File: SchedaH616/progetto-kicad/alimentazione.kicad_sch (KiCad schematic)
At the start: 53 parts, among them J103 DC-005-5A-2.0, J104 TYPE-C-31-M-12, U101 TPS56637RPAR, U103 TPS2121RUXR, U104 FUSB302BMPX, U105 SY6280AAC, U106 TPS259470ARPWR, U107 TPD2EUSB30ADRTR

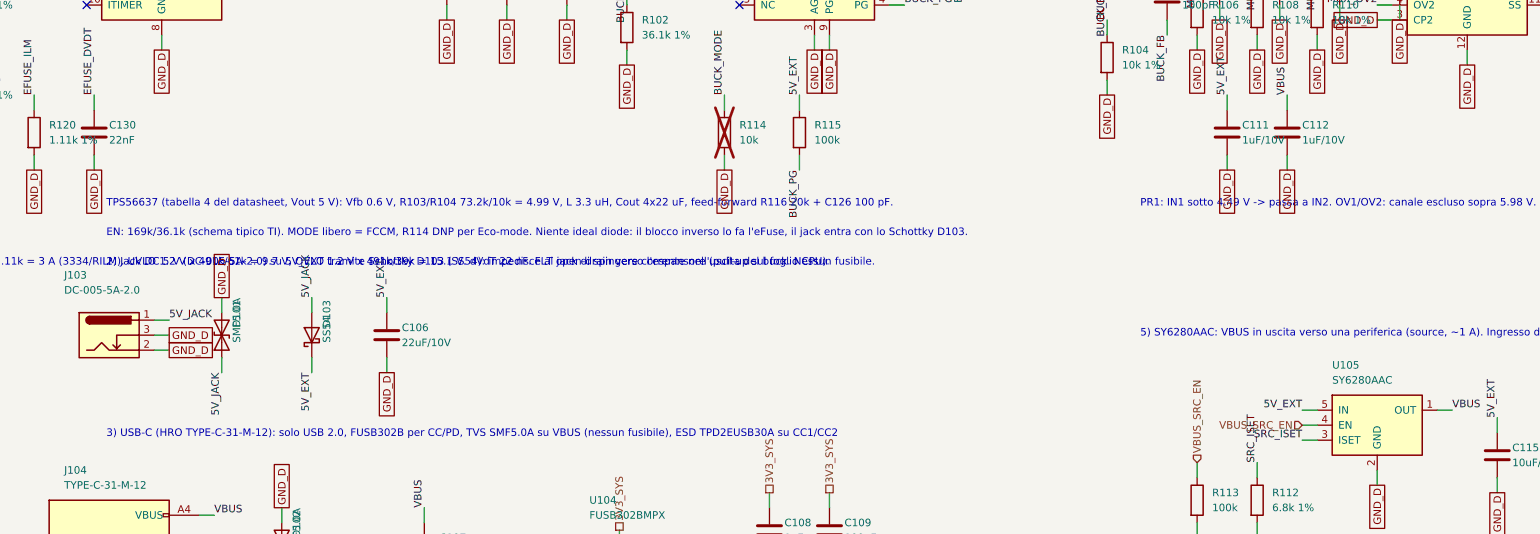
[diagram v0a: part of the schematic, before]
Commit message: SchedaH616: placement PCB 50x70 a 6 strati e modifiche allo schema
PCB (solo placement, niente piste), generato da generatori/build_pcb.sh:
- 50 x 70 mm, smussi 3 mm, 4 fori NPTH 2.2 mm con keepout, 6 strati
- H616 al centro, LPDDR4 sul lato DRAM, AXP313A vicino alla CPU, eMMC vicino ai pin PC
- connettori sui bordi, U.FL Wi-Fi e SMA GNSS su lati opposti
- disaccoppiamento di H616 e LPDDR4 sul bottom sotto le sfere
- regole: piste 5 mil, via-in-pad 0.25/0.15 sotto l'H616
- DRC: 0 violazioni (solo collegamenti da fare), parità schema/PCB ok

Schema (modifiche approvate):
- LPDDR4 confermata come scelta definitiva
- USB host di nuovo su USB-C solo host (Rp 22k, USBLC6-2, TPS2553)
- jack 5 V diretto su IN1 del TPS2121, tolto l'SS54, TPS56637 in Eco-mode
- LDO AP2112K-1.8 (C176944) dedicato a VCCQ eMMC e VCC_PC
- ERC 0

Libreria H616.pretty: serigrafia sui pad tolta, pioli di centraggio NPTH.

Co-Authored-By: Claude Opus 5.5 (1M context) <noreply@anthropic.com>
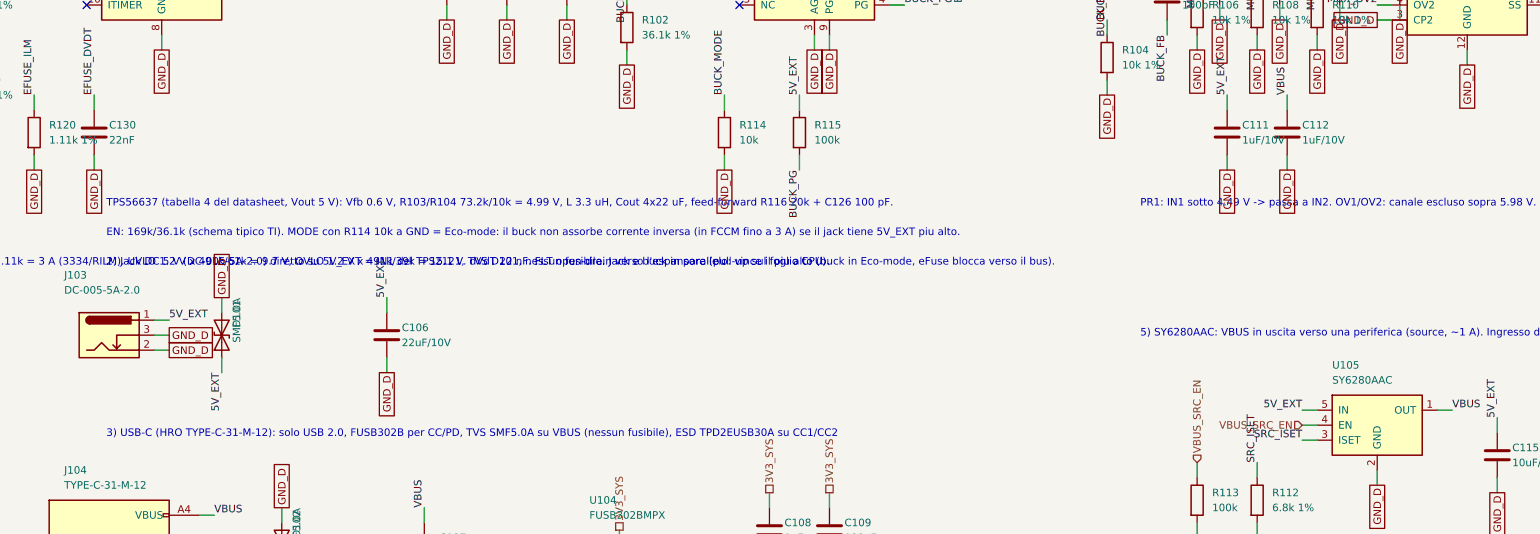
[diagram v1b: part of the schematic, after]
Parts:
- removed D103: SS54, Diode_SMD:D_SMC, symbol Device:D_Schottky
- R114: now fitted
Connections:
- net 5V_JACK is gone; now on net 5V_EXT: D101.1 (A1), J103.1
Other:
- note added: "2) Jack DC 5 V (DC-005-5A-2.0) diretto su 5V_EXT = IN1 del TPS2121, TVS D101, nessun fusibile. Jack e buck in parallelo: vince il piu alto (buck in Eco-mode, eFuse blocca verso il bus)."
- note added: "EN: 169k/36.1k (schema tipico TI). MODE con R114 10k a GND = Eco-mode: il buck non assorbe corrente inversa (in FCCM fino a 3 A) se il jack tiene 5V_EXT piu alto."
- note removed: "2) Jack DC 5 V (DC-005-5A-2.0) su 5V_EXT tramite Schottky D103 (SS54): impedisce al jack di spingere corrente nell'uscita del buck. Nessun fusibile."
- note removed: "EN: 169k/36.1k (schema tipico TI). MODE libero = FCCM, R114 DNP per Eco-mode. Niente ideal diode: il blocco inverso lo fa l'eFuse, il jack entra con lo Schottky D103."

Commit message: SchedaH616: secondo TPS2121 tra buck e jack, controlli dalla Orange Pi Zero2
- TPS2121 U108: IN1 = 5V_BUCK (priorita), IN2 = jack, uscita 5V_EXT verso U103 (IN2 = USB-C)
  PR1 4.49 V, CP2 a GND, OV 5.98 V, ILM 22.1k, ST con test point; priorita bus > jack > USB-C
- TPS56637 di nuovo in FCCM (R114 DNP): il buck ora e' isolato dal jack
- Dalla Orange Pi Zero2 v1.3: REXT 150k 1% ad AGND, AVCC e AC_AVCC 2.2 uF; AC_VRA1 su C17 confermato
- PCB aggiornato: U108 vicino a U103 e al jack
- ERC 0, parita' schema/PCB 0, DRC 0 (solo collegamenti da fare)

Co-Authored-By: Claude Opus 5.5 (1M context) <noreply@anthropic.com>
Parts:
- added C132: 100nF, Capacitor_SMD:C_0603_1608Metric, symbol Device:C
- added C133, C134: 1uF/10V, Capacitor_SMD:C_0603_1608Metric, symbol Device:C
- added C135: 10uF/10V, Capacitor_SMD:C_0805_2012Metric, symbol Device:C
- added R121: 32.4k 1%, Resistor_SMD:R_0603_1608Metric, symbol Device:R
- added R122, R124, R126: 10k 1%, Resistor_SMD:R_0603_1608Metric, symbol Device:R
- added R123, R125: 46.4k 1%, Resistor_SMD:R_0603_1608Metric, symbol Device:R
- added R127: 22.1k 1%, Resistor_SMD:R_0603_1608Metric, symbol Device:R
- added R128: 100k, Resistor_SMD:R_0603_1608Metric, symbol Device:R
- added TP101: MUX2_ST, TestPoint:TestPoint_Pad_D1.0mm, symbol Connector:TestPoint
- added U108: TPS2121RUXR, Package_DFN_QFN:Texas_VQFN-HR-12_2x2.5mm_P0.5mm, symbol H616:TPS2121
- R114: now not fitted
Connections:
- net 5V_EXT: now also C135.1, R128.1, U108.1 (OUT), U108.8 (OUT); no longer C104.1, C105.1, C106.1, C127.1, C128.1, D101.1 (A1), J103.1, L101.2, R103.1, R115.1, R116.1
- net GND_D: now also C132.2, C133.2, C134.2, C135.2, R122.2, R124.2, R126.2, R127.2, U108.12 (GND), U108.3 (CP2)
- new net 5V_BUCK: C104.1, C105.1, C127.1, C128.1, C133.1, L101.2, R103.1, R115.1, R116.1, R121.1, R123.1, U108.7 (IN1)
- new net 5V_JACK: C106.1, C134.1, D101.1 (A1), J103.1, R125.1, U108.2 (IN2)
- new net MUX2_ILM: R127.1, U108.10 (ILM)
- new net MUX2_OV1: R123.2, R124.1, U108.5 (OV1)
- new net MUX2_OV2: R125.2, R126.1, U108.4 (OV2)
- new net MUX2_PR1: R121.2, R122.1, U108.6 (PR1)
- new net MUX2_SS: C132.1, U108.11 (SS)
- new net MUX2_ST: R128.2, TP101.1, U108.9 (ST)
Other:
- note added: "1) VIN_SYS 12 V dal BUS_POWER (pin 24-26) -> eFuse TPS259470 (3 A, UVLO/OVLO, blocco inverso) -> buck TPS56637 12 -> 5 V / 6 A -> 5V_BUCK -> TPS2121 U108 (IN1, priorita)"
- note added: "2) Jack DC 5 V (DC-005-5A-2.0) su 5V_JACK, TVS D101, nessun fusibile. TPS2121 U108: IN1 = 5V_BUCK (bus 12 V) con priorita, IN2 = jack. Uscita 5V_EXT -> IN1 di U103."
- note added: "4) Power mux TPS2121 U103: IN1 5V_EXT (uscita di U108: bus o jack) con priorita, IN2 VBUS USB-C. Uscita 5V_SYS verso AXP313A e 3V3_PERI"
- note added: "EN: 169k/36.1k (schema tipico TI). MODE libero = FCCM (R114 DNP): frequenza fissa, ripple basso vicino al GNSS. Il jack e' separato dal TPS2121 U108, niente corrente inversa nel buck."
- note added: "Priorita: bus 12 V (buck) > jack > USB-C. Il bus e' l'alimentazione di esercizio, il jack serve al banco, l'USB-C e' l'ultima risorsa (1.5-3 A)."
- note added: "U108 (datasheet TPS2121 SLVSEA3F): PR1 = 1.06 V x (32.4k+10k)/10k = 4.49 V -> sotto passa al jack; CP2 a GND = priorita fissa su IN1; OV 5.98 V; ILM 22.1k = 4-5 A; ST (basso = uscita dal jack, IN2) con 100k e test point TP101."
- note removed: "1) VIN_SYS 12 V dal BUS_POWER (pin 24-26) -> eFuse TPS259470 (3 A, UVLO/OVLO, blocco inverso) -> buck TPS56637 12 -> 5 V / 6 A -> 5V_EXT"
- note removed: "2) Jack DC 5 V (DC-005-5A-2.0) diretto su 5V_EXT = IN1 del TPS2121, TVS D101, nessun fusibile. Jack e buck in parallelo: vince il piu alto (buck in Eco-mode, eFuse blocca verso il bus)."
- note removed: "4) Power mux TPS2121: IN1 5V_EXT (jack o VIN_SYS) con priorita, IN2 VBUS USB-C. Uscita 5V_SYS verso AXP313A e 3V3_PERI"
- note removed: "EN: 169k/36.1k (schema tipico TI). MODE con R114 10k a GND = Eco-mode: il buck non assorbe corrente inversa (in FCCM fino a 3 A) se il jack tiene 5V_EXT piu alto."

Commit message: SchedaH616: eFuse TPS259470 eliminato
- tolti U106 TPS259470 e i suoi componenti (partitore UVLO/OVLO, RILM, dVdT, 1 uF d'ingresso) e il footprint RPW dalla libreria
- VIN_SYS dal BUS_POWER direttamente all'ingresso del TPS56637 (restano C101/C102 10 uF e C125 100 nF)
- ingresso 12 V senza limite di corrente, OVP ne' blocco inverso; nessuna TVS sui 12 V
- P17 del TCA6416A ora libera; documenti aggiornati
- ERC 0, parita' 0, DRC 0 (solo collegamenti da fare)

Co-Authored-By: Claude Opus 5.5 (1M context) <noreply@anthropic.com>
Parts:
- removed C130: 22nF, Capacitor_SMD:C_0603_1608Metric, symbol Device:C
- removed C131: 1uF/25V, Capacitor_SMD:C_0805_2012Metric, symbol Device:C
- removed R117: 430k 1%, Resistor_SMD:R_0603_1608Metric, symbol Device:R
- removed R118: 22k 1%, Resistor_SMD:R_0603_1608Metric, symbol Device:R
- removed R119: 39k 1%, Resistor_SMD:R_0603_1608Metric, symbol Device:R
- removed R120: 1.11k 1%, Resistor_SMD:R_0603_1608Metric, symbol Device:R
- removed U106: TPS259470ARPWR, H616:Texas_RPW0010A_VQFN-HR-10_2x2mm_P0.5mm, symbol H616:TPS259470
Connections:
- net VIN_12V is gone; now on net VIN_SYS: C101.1, C102.1, C125.1, R101.1, U101.8 (VIN)
- no-connect marks 7 -> 5
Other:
- note added: "1) VIN_SYS 12 V dal BUS_POWER (pin 24-26) direttamente nel buck TPS56637 (eFuse tolto su richiesta di Michele: niente limite di corrente, OVP ne' blocco inverso) 12 -> 5 V / 6 A -> 5V_BUCK -> TPS2121 U108 (IN1, priorita)"
- note removed: "1) VIN_SYS 12 V dal BUS_POWER (pin 24-26) -> eFuse TPS259470 (3 A, UVLO/OVLO, blocco inverso) -> buck TPS56637 12 -> 5 V / 6 A -> 5V_BUCK -> TPS2121 U108 (IN1, priorita)"
- note removed: "eFuse: RILM 1.11k = 3 A (3334/RILM). UVLO 1.2 V x 491k/61k = 9.7 V, OVLO 1.2 V x 491k/39k = 15.1 V. dVdT 22 nF. FLT open-drain verso l'espansore (pull-up sul foglio CPU)."

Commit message: SchedaH616: RK3568 + RK809-5 + TCS4525 + DDR4, placement 50x70
- SoC Allwinner H616 -> Rockchip RK3568 (FCBGA636L, LCSC C2938930): ball map dal pinout
  Rockchip V1.1, verificata sulla tabella 2-1 del datasheet V1.2 (636/636); footprint
  generato (gen_fp.py), confrontato con EasyEDA C2938930
- PMIC AXP313A -> RK809-5 (C2939628) come Rockchip AIoT REF V1.1 / ROCK 3A; TCS4525 per
  VDD_CPU su I2C0 (0x1C); BUCK4 su VDD_NPU (sull'RK809-5 parte spento: non puo' fare il 3.3 V)
- LPDDR4 -> DDR4 x16 K4AAG165WA-BCWE (C2920140) sul canale A, point-to-point, niente VTT,
  VPP da AP2112K-2.5, ZQ 240R, DDR_RZQ del SoC 120R (Hardware Design Guide)
- eMMC su EMMC 8 bit (VCCIO2 1.8 V), microSD su SDMMC0, AP6256 su SDMMC2 + UART8,
  RTL8211F su GMAC0 RGMII (22R TX al SoC e RX al PHY), console UART2_M0, USB-C su OTG0
- Recovery su SARADC_VIN0, reset sulla rete RESETn; TCA6416A tolto
- Bus MIKILAB: BUS_POWER su SPI3_M1, MAIN su SPI2_M1 (CS del DAC su cs-gpios)
- progetto rinominato SchedaRK3568, libreria di progetto Scheda; script portabili Linux/macOS
- ERC 0, parita' 0, DRC 0 (solo collegamenti da fare); placement 439/439

Co-Authored-By: Claude Opus 5.5 (1M context) <noreply@anthropic.com>
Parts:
- removed U101: TPS56637RPAR, H616:Texas_RPA0010A_VQFN-HR-10_3x3mm, symbol H616:TPS56637
- removed U103, U108: TPS2121RUXR, Package_DFN_QFN:Texas_VQFN-HR-12_2x2.5mm_P0.5mm, symbol H616:TPS2121
- removed U105: SY6280AAC, Package_TO_SOT_SMD:SOT-23-5, symbol H616:SY6280AAC
- added C136: 100nF, Capacitor_SMD:C_0402_1005Metric, symbol Device:C
- added R129: 10k 1%, Resistor_SMD:R_0402_1005Metric, symbol Device:R
- added R130: 15k 1%, Resistor_SMD:R_0402_1005Metric, symbol Device:R
- added U101: TPS56637RPAR, Scheda:Texas_RPA0010A_VQFN-HR-10_3x3mm, symbol Scheda:TPS56637
- added U103, U108: TPS2121RUXR, Package_DFN_QFN:Texas_VQFN-HR-12_2x2.5mm_P0.5mm, symbol Scheda:TPS2121
- added U105: SY6280AAC, Package_TO_SOT_SMD:SOT-23-5, symbol Scheda:SY6280AAC
- C103, C108, C109, C110, C111, C112, C114, C125, C126, C132, C133, C134: footprint Capacitor_SMD:C_0603_1608Metric -> Capacitor_SMD:C_0402_1005Metric
- R101, R102, R103, R104, R105, R106, R107, R108, R109, R110, R111, R112, R113, R114, R115, R116, R121, R122, R123, R124, R125, R126, R127, R128: footprint Resistor_SMD:R_0603_1608Metric -> Resistor_SMD:R_0402_1005Metric
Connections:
- net 5V_BUCK: now also U108.7 (IN1)
- net 5V_EXT: now also U103.7 (IN1), U105.5 (IN), U108.1 (OUT), U108.8 (OUT)
- net 5V_JACK: now also U108.2 (IN2)
- net 5V_SYS: now also U103.1 (OUT), U103.8 (OUT)
- net BUCK_BST: now also U101.7 (BOOT)
- net BUCK_EN: now also U101.1 (EN)
- net BUCK_FB: now also U101.2 (FB)
- net BUCK_MODE: now also U101.10 (MODE)
- net BUCK_PG: now also U101.4 (PG)
- net BUCK_SW: now also U101.6 (SW)
- net GND_D: now also C136.2, R130.2, U101.3 (AGND), U101.9 (PGND), U103.12 (GND), U103.3 (CP2), U105.2 (GND), U108.12 (GND), U108.3 (CP2)
- net MUX2_ILM: now also U108.10 (ILM)
- net MUX2_OV1: now also U108.5 (OV1)
- net MUX2_OV2: now also U108.4 (OV2)
- net MUX2_PR1: now also U108.6 (PR1)
- net MUX2_SS: now also U108.11 (SS)
- net MUX2_ST: now also U108.9 (ST)
- net MUX_ILM: now also U103.10 (ILM)
- net MUX_OV1: now also U103.5 (OV1)
- net MUX_OV2: now also U103.4 (OV2)
- net MUX_PR1: now also U103.6 (PR1)
- net MUX_SS: now also U103.11 (SS)
- net PWR_SRC_ST: now also U103.9 (ST)
- net SRC_ISET: now also U105.3 (ISET)
- net VBUS: now also R129.1, U103.2 (IN2), U105.1 (OUT)
- net VBUS_SRC_EN: now also U105.4 (EN)
- net VIN_SYS: now also U101.8 (VIN)
- net 3V3_SYS renamed VCC3V3_SYS
- net PMU-SCK renamed I2C1_SCL
- net PMU-SDA renamed I2C1_SDA
- new net OTG_VBUSDET: C136.1, R129.2, R130.1
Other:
- note added: "1) VIN_SYS 12 V dal BUS_POWER (pin 24-26) -> buck TPS56637 12 -> 5 V / 6 A -> 5V_BUCK -> TPS2121 U108 (IN1, priorita). Niente eFuse e niente fusibile."
- note added: "4) Power mux TPS2121 U103: IN1 5V_EXT (uscita di U108: bus o jack) con priorita, IN2 VBUS USB-C. Uscita 5V_SYS verso TPS563201 (VCC3V3_SYS), TCS4525 (VDD_CPU) e TPS2553"
- note added: "FUSB302B (0x22): VDD da VCC3V3_SYS, I2C1 dell'RK3568 (GPIO0_B3/B4, PMUIO2 3.3 V) con pull-up 2.2k a VCC3V3_PMU e INT_N 10k a VCC_3V3 sul foglio CPU."
- note added: "Ilim = 6800 / R112 = 1 A. R113: uscita spenta finche Linux non abilita VBUS_SRC_EN (GPIO0_A5, comandato da tcpm)."
- note added: "Senza eFuse il buck vede direttamente il BUS_POWER: niente limite di corrente, UVLO/OVLO e blocco inverso sui 12 V (protezione a carico del modulo Power)."
- note added: "USB3_OTG0_VBUSDET (M24): VBUS x 15k/(10k+15k) = 3.0 V con 100 nF (Hardware Design Guide RK3568: 2.7-3.3 V, tip. 3.0 V). Serve al flash con rkdeveloptool (modo device)."
- note removed: "1) VIN_SYS 12 V dal BUS_POWER (pin 24-26) direttamente nel buck TPS56637 (eFuse tolto su richiesta di Michele: niente limite di corrente, OVP ne' blocco inverso) 12 -> 5 V / 6 A -> 5V_BUCK -> TPS2121 U108 (IN1, priorita)"
- note removed: "4) Power mux TPS2121 U103: IN1 5V_EXT (uscita di U108: bus o jack) con priorita, IN2 VBUS USB-C. Uscita 5V_SYS verso AXP313A e 3V3_PERI"
- note removed: "FUSB302B: I2C condivisa con AXP313A ed espansore su S_TWI0 (PL0/PL1, 1.8 V: VIH 1.32 V, pull-up 1.71 V..VDD da datasheet). Pull-up 2.2k e INT_N 10k a VCC-1V8 sul foglio CPU."
- note removed: "Ilim = 6800 / R112 = 1 A. R113: uscita spenta finche Linux non abilita VBUS_SRC_EN (comandato da tcpm)."
